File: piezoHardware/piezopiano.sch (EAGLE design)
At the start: 46 parts, among them J1 CON2, Q1 BSS123, Q2 BSS123, Q3 BSS123, Q4 BSS123, Q5 BSS123, Q6 BSS123, Q7 BSS123, Q8 BSS123, U1 MEGA328PB-AU

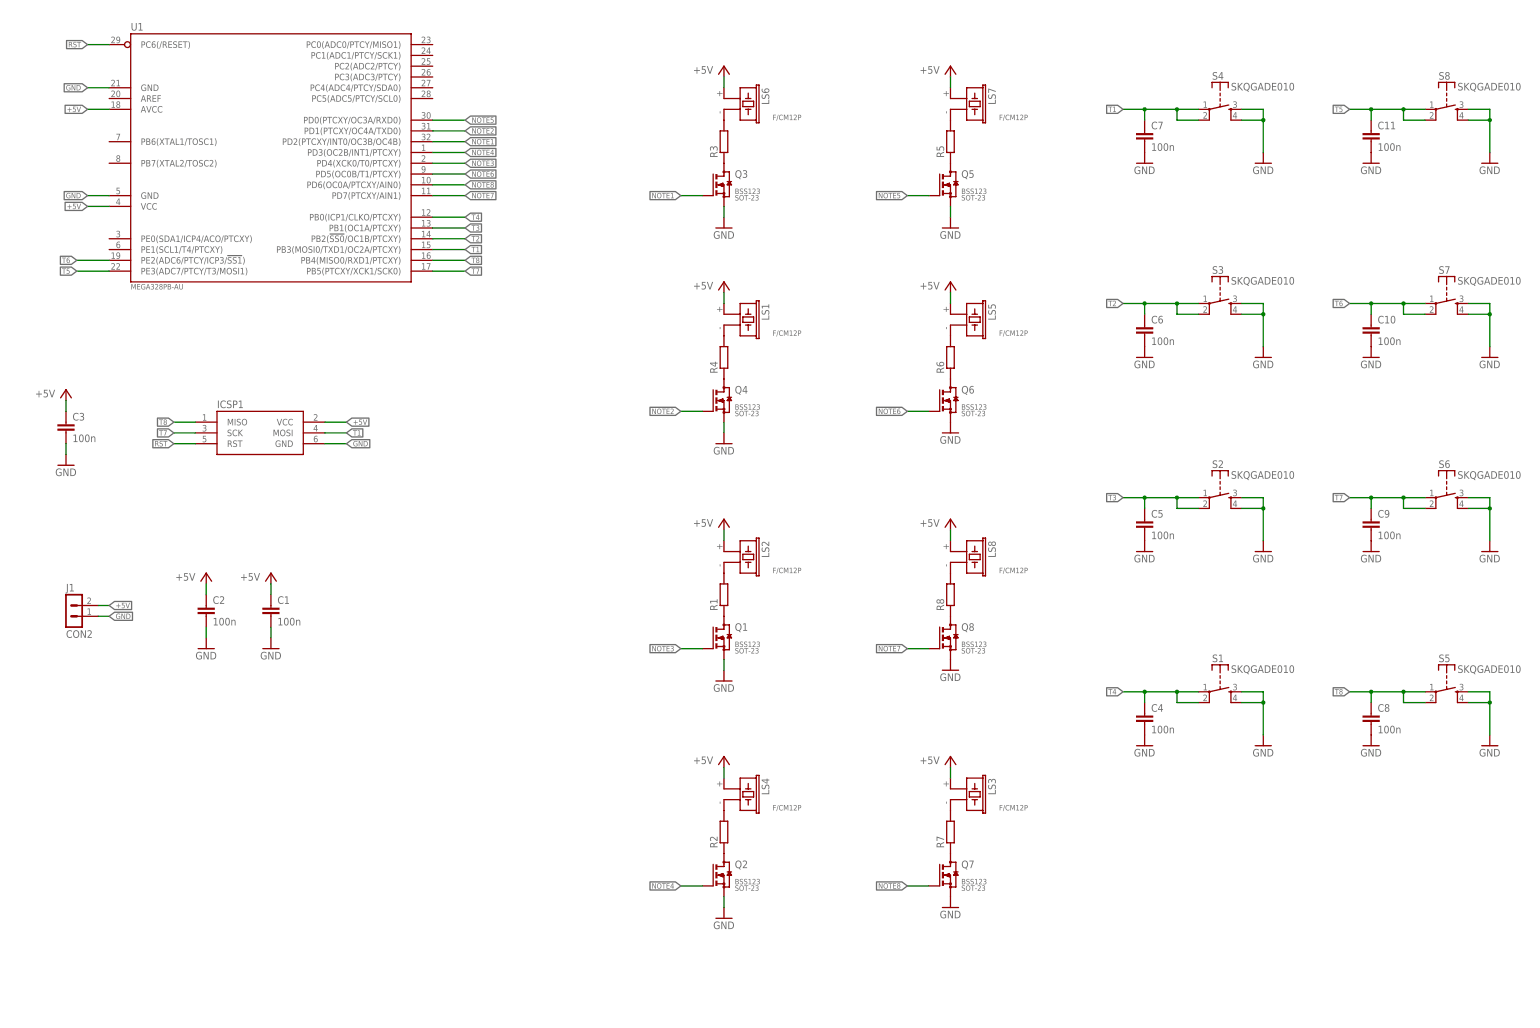
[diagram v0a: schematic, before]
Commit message: LDO added
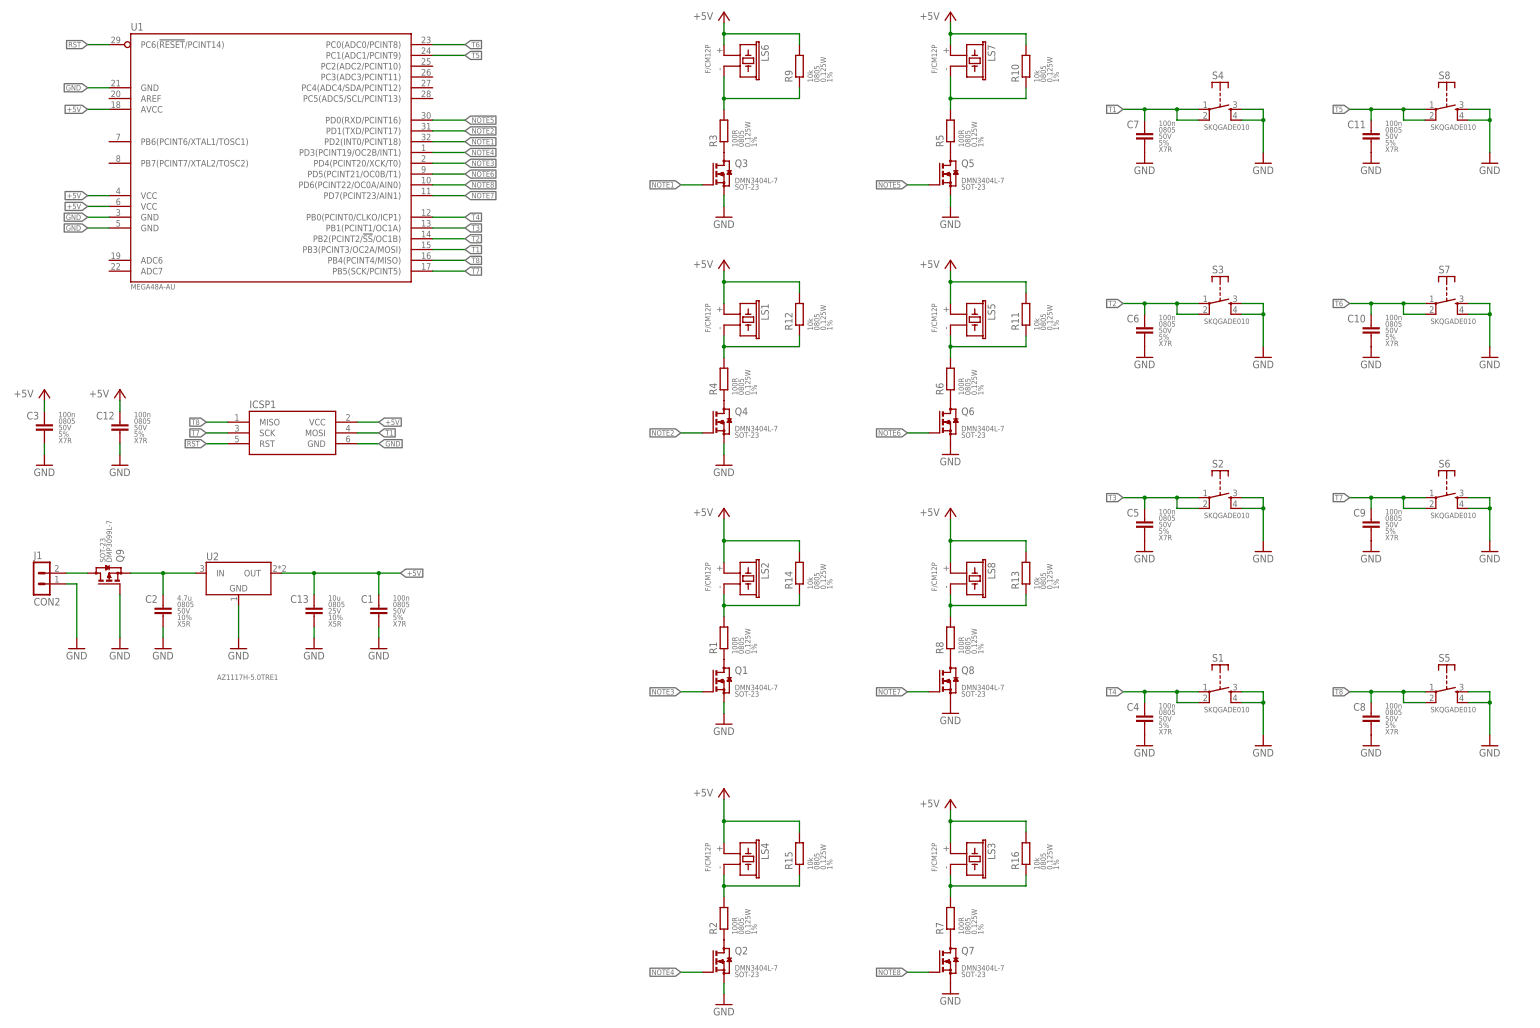
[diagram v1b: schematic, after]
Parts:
- added C12: 100n, zaan-Capacitors:100NF-0805-50V-5%
- added C13: 10u, zaan-Capacitors:10UF-0805-25V-10%
- added Q9: DMP3099L, zaan-Discrete:DMP3099L
- added R10, R11, R12, R13, R14, R15, R16, R9: 10k, zaan-Resistors:10KOHM-0805-1/8W-1%
- added U2: AZ1117H-5.0TRE1, zaan-IC-Power:AZ1117H-5.0TRE1
- C1, C10, C11, C3, C4, C5, C6, C7, C8, C9: device rcl:C-EUC0805 -> zaan-Capacitors:100NF-0805-50V-5%
- C2: value 100n -> 4.7u; device rcl:C-EUC0805 -> zaan-Capacitors:4.7UF-0805-50V-10%
- LS1, LS2, LS3, LS4, LS5, LS6, LS7, LS8: device Custom:F/CM12P -> zaan-Electromechanical:F/CM12P
- Q1, Q2, Q3, Q4, Q5, Q6, Q7, Q8: value BSS123 -> DMN3404L; device Custom:BSS123 -> zaan-Discrete:DMN3404L
- R1, R2, R3, R4, R5, R6, R7, R8: value (none) -> 100R; device rcl:R-EU_R0805 -> zaan-Resistors:100OHM-0805-1/8W-1%
- S1, S2, S3, S4, S5, S6, S7, S8: device Custom:SKQGADE010 -> zaan-Electromechanical:SKQGADE010
- U1: value MEGA328PB-AU -> MEGA48A-AU; device Custom:MEGA328PB-AU -> zaan-IC-Microcontroller:MEGA48A-AU
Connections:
- new net N$17: C2.1, Q9.S, U2.IN
- new net N$18: LS6.2, R3.2, R9.1
- net +5V: now also C12.1, C13.1, R10.2, R11.2, R12.2, R13.2, R14.2, R15.2, R16.2, R9.2, U1.VCC@2, U2.OUT; no longer C2.1, J1.2
- net GND: now also C12.2, C13.2, Q9.G, U1.GND@2, U2.GND
- net N$1: now also J1.2, Q9.D; no longer LS6.2, R3.2
- net N$10: now also R12.1
- net N$11: now also R14.1
- net N$13: now also R10.1
- net N$15: now also R13.1
- net N$16: now also R16.1
- net N$4: now also R15.1
- net N$6: now also R11.1
- net NOTE1: now also U1.PD2(INT0/PCINT18); no longer U1.PD2(PTCXY/INT0/OC3B/OC4B)
- net NOTE2: now also U1.PD1(TXD/PCINT17); no longer U1.PD1(PTCXY/OC4A/TXD0)
- net NOTE3: now also U1.PD4(PCINT20/XCK/T0); no longer U1.PD4(XCK0/T0/PTCXY)
- net NOTE4: now also U1.PD3(PCINT19/OC2B/INT1); no longer U1.PD3(OC2B/INT1/PTCXY)
- net NOTE5: now also U1.PD0(RXD/PCINT16); no longer U1.PD0(PTCXY/OC3A/RXD0)
- net NOTE6: now also U1.PD5(PCINT21/OC0B/T1); no longer U1.PD5(OC0B/T1/PTCXY)
- net NOTE7: now also U1.PD7(PCINT23/AIN1); no longer U1.PD7(PTCXY/AIN1)
- net NOTE8: now also U1.PD6(PCINT22/OC0A/AIN0); no longer U1.PD6(OC0A/PTCXY/AIN0)
- net RST: now also U1.PC6(!RESET!/PCINT14); no longer U1.PC6(/RESET)
- net T1: now also U1.PB3(PCINT3/OC2A/MOSI); no longer U1.PB3(MOSI0/TXD1/OC2A/PTCXY)
- net T2: now also U1.PB2(PCINT2/!SS!/OC1B); no longer U1.PB2(!SS0!/OC1B/PTCXY)
- net T3: now also U1.PB1(PCINT1/OC1A); no longer U1.PB1(OC1A/PTCXY)
- net T4: now also U1.PB0(PCINT0/CLKO/ICP1); no longer U1.PB0(ICP1/CLKO/PTCXY)
- net T5: now also U1.PC1(ADC1/PCINT9); no longer U1.PE3(ADC7/PTCY/T3/MOSI1)
- net T6: now also U1.PC0(ADC0/PCINT8); no longer U1.PE2(ADC6/PTCY/ICP3/!SS1!)
- net T7: now also U1.PB5(SCK/PCINT5); no longer U1.PB5(PTCXY/XCK1/SCK0)
- net T8: now also U1.PB4(PCINT4/MISO); no longer U1.PB4(MISO0/RXD1/PTCXY)
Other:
- moved on the sheet: C1, C2, C3, ICSP1, J1, LS2, LS3, LS4, LS6, LS7, LS8, Q1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

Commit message: Partly finished layout
Missing crystal
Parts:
- removed C11, C12: 100n, zaan-Capacitors:100NF-0805-50V-5%
- added C100: 4.7u, zaan-Capacitors:4.7UF-0805-50V-10%
- added C102: 100n, zaan-Capacitors:100NF-0805-50V-5%
- C2: value 4.7u -> 100n; device zaan-Capacitors:4.7UF-0805-50V-10% -> zaan-Capacitors:100NF-0805-50V-5%
- R1, R3, R5, R7: value 100R -> 10k; device zaan-Resistors:100OHM-0805-1/8W-1% -> zaan-Resistors:10KOHM-0805-1/8W-1%
- R10, R12, R14, R16: value 10k -> 100R; device zaan-Resistors:10KOHM-0805-1/8W-1% -> zaan-Resistors:100OHM-0805-1/8W-1%
- renumbered C13 to C101, Q9 to Q100, U2 to U100
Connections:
- net +5V: now also C102.1, C2.1, R1.2, R3.2, R5.2, R7.2; no longer C12.1, C3.1, R10.2, R12.2, R14.2, R16.2
- net GND: now also C100.2, C102.2; no longer C11.2, C12.2
- net N$10: now also LS3.2, R7.1, R8.2; no longer LS1.2, R12.1, R4.2
- net N$11: now also LS5.2, R1.1, R2.2; no longer LS2.2, R1.2, R14.1
- net N$12: now also R4.1; no longer R2.1
- net N$13: now also LS8.2, R10.2, R9.1; no longer LS7.2, R10.1, R5.2
- net N$14: now also R12.1; no longer R6.1
- net N$15: now also LS4.2, R15.1, R16.2; no longer LS8.2, R13.1, R8.2
- net N$16: now also LS6.2, R13.1, R14.2; no longer LS3.2, R16.1, R7.2
- net N$17: now also C100.1; no longer C2.1
- net N$18: now also LS7.2, R5.1, R6.2; no longer LS6.2, R3.2, R9.1
- net N$2: now also R8.1; no longer R4.1
- net N$3: now also R2.1; no longer R1.1
- net N$4: now also LS2.2, R3.1, R4.2; no longer LS4.2, R15.1, R2.2
- net N$5: now also R10.1; no longer R5.1
- net N$6: now also LS1.2, R12.2; no longer LS5.2, R6.2
- net N$7: now also R16.1; no longer R8.1
- net N$8: now also R14.1; no longer R7.1
- net N$9: now also R6.1; no longer R3.1
- net T1: now also C6.1; no longer C7.1
- net T2: now also C5.1; no longer C6.1
- net T3: now also C4.1; no longer C5.1
- net T4: now also C3.1; no longer C4.1
- net T5: now also C10.1; no longer C11.1
- net T6: now also C9.1; no longer C10.1
- net T7: now also C8.1; no longer C9.1
- net T8: now also C7.1; no longer C8.1
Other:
- moved on the sheet: C1, C10, C2, C3, C4, C5, C6, C7, C8, C9, LS1, LS2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

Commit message: Minor part update
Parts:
- U100: value AZ1117H-5.0TRE1 -> AP7381-50Y-13; device zaan-IC-Power:AZ1117H-5.0TRE1 -> zaan-IC-Power:AP7381-50Y-13
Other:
- moved on the sheet: C100, C101, C102, J1, Q100, U100
